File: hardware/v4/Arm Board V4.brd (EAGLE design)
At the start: 108 x 50.8 mm, 38 parts, among them IC3 L6206D, P1 STELLARIS-LAUNCHPADSTELLARIS-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, U1 SN74LS241DW, U2 XBEE-1B3

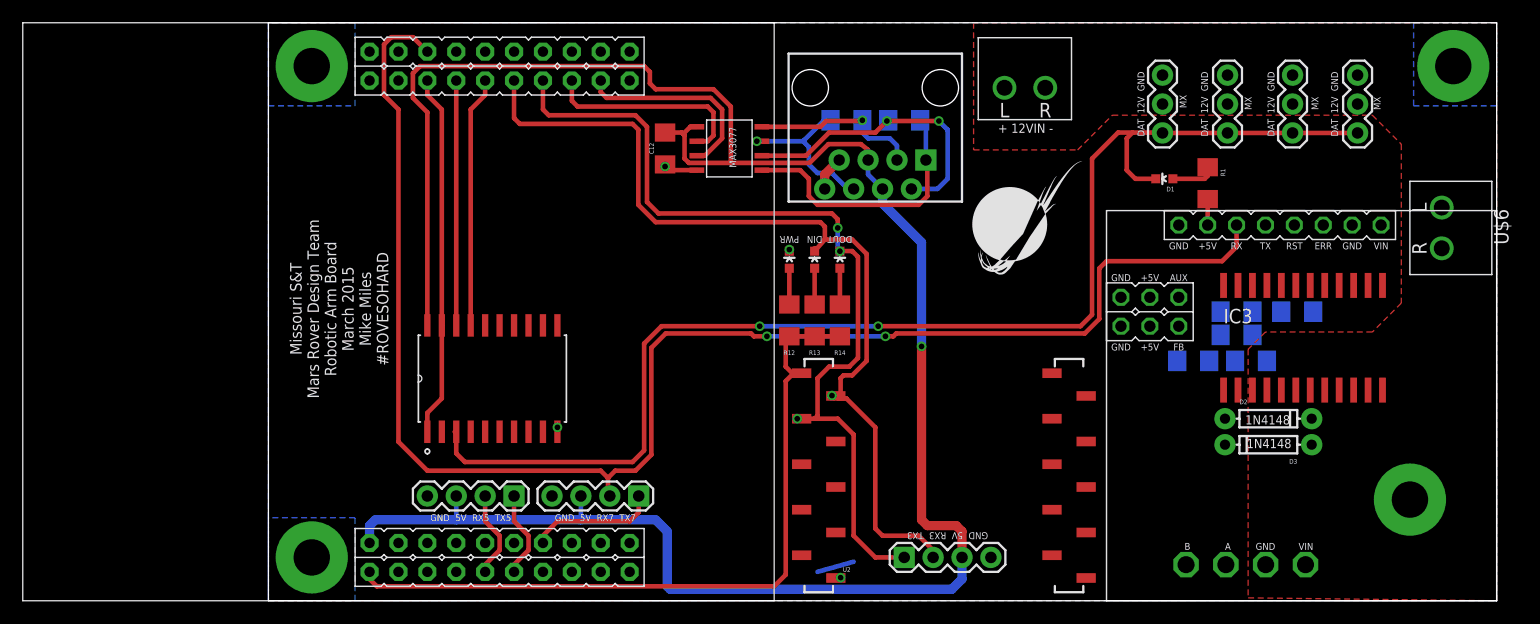
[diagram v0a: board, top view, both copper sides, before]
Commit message: arm board
added parts to allow linear actuator control with H-bridge in case servo
driver fails
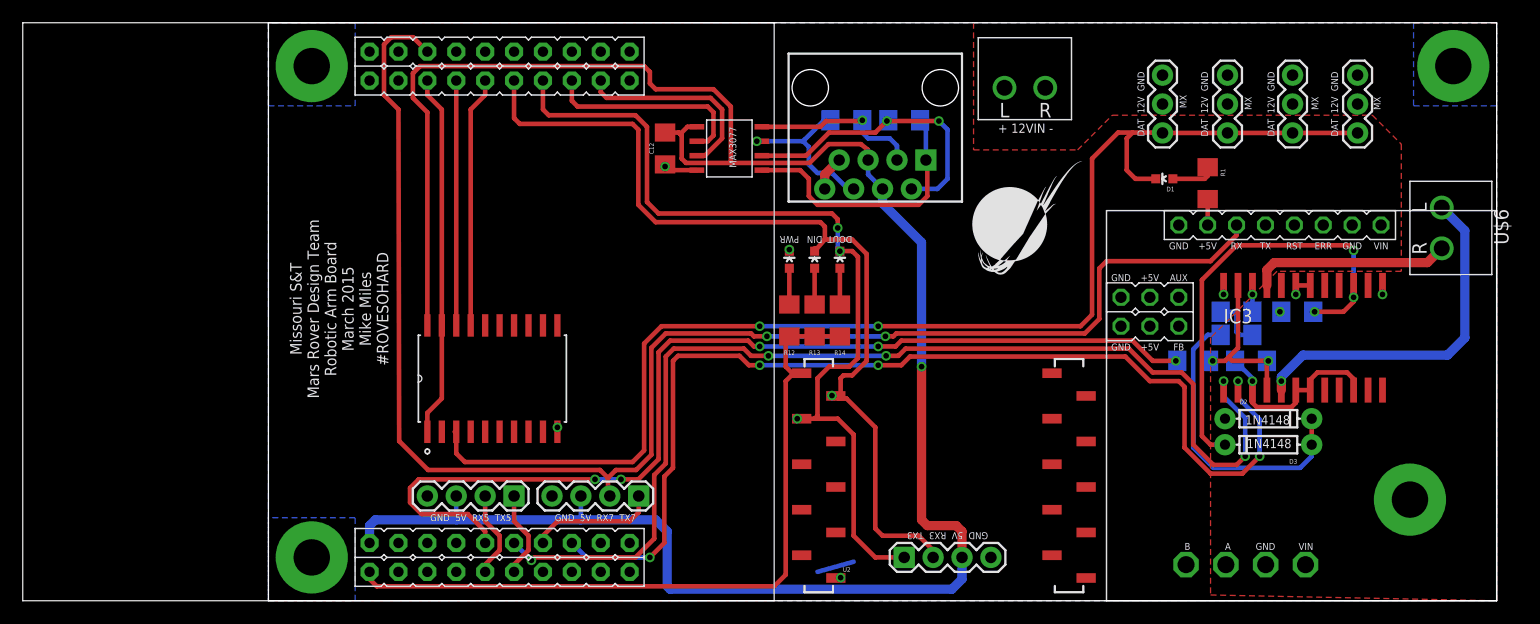
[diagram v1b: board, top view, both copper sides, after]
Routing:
- net IN1_A: track 0.00 -> 97.8 mm, vias 0 -> 5
- net IN2_A: track 0.00 -> 94.1 mm, vias 0 -> 5
- net EN_A: track 0.00 -> 89.7 mm, vias 0 -> 5
- net VBOOT: track 0.00 -> 40.3 mm, vias 0 -> 3
- net A1: track 0.00 -> 31.0 mm, vias 0 -> 1
- net N$17: track 0.00 -> 26.4 mm, vias 0 -> 1
- net GND: track 10.5 -> 31.2 mm, vias 4 -> 8
- net A2: track 0.00 -> 17.5 mm
- net OCD_A: track 0.00 -> 14.7 mm, vias 0 -> 2
- net N$18: track 0.00 -> 4.53 mm
- net N$19: track 0.00 -> 2.32 mm, vias 0 -> 1
- net RX_7: track 135.3 -> 134.6 mm
- net +12V: track 0.00 -> 0.12 mm, vias 0 -> 1

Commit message: about to reroute brd
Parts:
- moved R1 3.86 mm to (78.9, 35.6), turned to 0 degrees
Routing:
- net +5V: track 189.4 -> 191.2 mm
- net N$13: track 3.93 -> 2.65 mm
- net DDATA_1: track 113.5 -> 114.7 mm
- net TX_3: track 77.5 -> 78.5 mm
- net RX_3: track 80.9 -> 81.6 mm
- net GND: track 31.2 -> 31.7 mm
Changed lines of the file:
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@@
 <layer number="21" name="tPlace" color="7" fill="1" visible="yes" active="yes"/>
 <layer number="22" name="bPlace" color="7" fill="1" visible="yes" active="yes"/>
-<layer number="23" name="tOrigins" color="15" fill="1" visible="no" active="yes"/>
-<layer number="24" name="bOrigins" color="15" fill="1" visible="no" active="yes"/>
+<layer number="23" name="tOrigins" color="15" fill="1" visible="yes" active="yes"/>
+<layer number="24" name="bOrigins" color="15" fill="1" visible="yes" active="yes"/>
 <layer number="25" name="tNames" color="7" fill="1" visible="no" active="yes"/>
 <layer number="26" name="bNames" color="7" fill="1" visible="no" active="yes"/>
@@
 </element>
 <element name="U$1" library="MRDT-RoboticArm" package="TORXIS_BREAKOUT" value="TORXIS_BREAKOUT" x="107.95" y="0" rot="R90"/>
-<element name="R1" library="SparkFun-Resistors" package="1206" value="1k" x="82.55" y="36.703" rot="R270"/>
+<element name="R1" library="SparkFun-Resistors" package="1206" value="1k" x="78.867" y="35.56"/>
 <element name="D1" library="SparkFun-LED" package="LED-0603" value="RED" x="78.74" y="37.084" rot="R90">
 <attribute name="PROD_ID" value="DIO-00819" x="78.74" y="37.084" size="1.778" layer="27" rot="R90" display="off"/>
@@
 <via x="34.8615" y="38.1635" extent="1-16" drill="0.5"/>
 <wire x1="34.8615" y1="38.351" x2="34.8615" y2="38.1635" width="0.4064" layer="1"/>
-<via x="25.4" y="15.24" extent="1-16" drill="0.5"/>
-<wire x1="25.4" y1="15.24" x2="25.4" y2="14.85265" width="0.4064" layer="1"/>
-<via x="50.292" y="2.032" extent="1-16" drill="0.5"/>
-<wire x1="50.292" y1="2.032" x2="49.902" y2="2.032" width="0.4064" layer="1"/>
+<via x="25.4" y="15.5575" extent="1-16" drill="0.5"/>
+<wire x1="25.4" y1="15.5575" x2="25.4" y2="14.85265" width="0.4064" layer="1"/>
+<via x="49.276" y="2.032" extent="1-16" drill="0.5"/>
+<wire x1="49.276" y1="2.032" x2="49.902" y2="2.032" width="0.4064" layer="1"/>
 <wire x1="49.902" y1="2.032" x2="49.87" y2="2" width="0.4064" layer="1"/>
 <wire x1="48.895" y1="36.195" x2="48.895" y2="37.465" width="0.8128" layer="1"/>
@@
 <contactref element="R1" pad="2"/>
 <contactref element="U$1" pad="+5V_OUT"/>
-<wire x1="82.55" y1="33.02" x2="82.55" y2="35.303" width="0.4064" layer="1"/>
 <wire x1="37.6555" y1="41.656" x2="36.83" y2="41.656" width="0.4064" layer="1"/>
 <wire x1="27.432" y1="9.23925" x2="27.432" y2="9.17575" width="0.4064" layer="16"/>
@@
 <wire x1="34.8645" y1="41.148" x2="34.8615" y2="41.151" width="0.4064" layer="1"/>
 <wire x1="36.83" y1="41.656" x2="36.195" y2="41.021" width="0.4064" layer="1"/>
-<wire x1="57.404" y1="31.496" x2="82.55" y2="33.02" width="0" layer="19" extent="16-16"/>
+<wire x1="82.55" y1="33.02" x2="82.55" y2="34.29" width="0.4064" layer="1"/>
+<wire x1="82.55" y1="34.29" x2="81.28" y2="35.56" width="0.4064" layer="1"/>
+<wire x1="81.28" y1="35.56" x2="80.267" y2="35.56" width="0.4064" layer="1"/>
+<wire x1="57.404" y1="31.496" x2="80.267" y2="35.56" width="0" layer="19" extent="1-16"/>
 </signal>
 <signal name="+12V">
@@
 <wire x1="49.65" y1="17.78" x2="49.87" y2="18" width="0.4064" layer="1"/>
 <wire x1="21.59" y1="45.72" x2="21.59" y2="42.418" width="0.4064" layer="1"/>
-<wire x1="49.53" y1="17.78" x2="49.53" y2="18.034" width="0.4064" layer="1"/>
-<via x="49.53" y="18.034" extent="1-16" drill="0.5"/>
+<wire x1="49.53" y1="17.78" x2="49.276" y2="18.034" width="0.4064" layer="1"/>
+<via x="49.276" y="18.034" extent="1-16" drill="0.5"/>
 <wire x1="22.098" y1="41.91" x2="21.59" y2="42.418" width="0.4064" layer="1"/>
 <wire x1="32.004" y1="41.91" x2="22.098" y2="41.91" width="0.4064" layer="1"/>
-<wire x1="49.784" y1="18.034" x2="49.53" y2="18.034" width="0.4064" layer="1"/>
-<wire x1="49.53" y1="18.034" x2="50.292" y2="18.034" width="0.4064" layer="1"/>
+<wire x1="49.784" y1="18.034" x2="49.276" y2="18.034" width="0.4064" layer="1"/>
+<wire x1="49.276" y1="18.034" x2="50.292" y2="18.034" width="0.4064" layer="1"/>
 <wire x1="50.292" y1="18.034" x2="50.292" y2="19.558" width="0.4064" layer="1"/>
 <wire x1="50.292" y1="19.558" x2="50.546" y2="19.812" width="0.4064" layer="1"/>
@@
 <wire x1="46.87" y1="16" x2="47.5" y2="16" width="0.4064" layer="1"/>
 <wire x1="46.87" y1="16" x2="46.484" y2="16" width="0.4064" layer="1"/>
-<wire x1="46.484" y1="16" x2="46.482" y2="16.002" width="0.4064" layer="1"/>
-<via x="46.482" y="16.002" extent="1-16" drill="0.5"/>
+<wire x1="46.484" y1="16" x2="47.498" y2="16.002" width="0.4064" layer="1"/>
+<via x="47.498" y="16.002" extent="1-16" drill="0.5"/>
 <wire x1="50.04" y1="16" x2="48.006" y2="16" width="0.4064" layer="1"/>
 <wire x1="48.006" y1="16" x2="47.5" y2="16" width="0.4064" layer="1"/>
@@
 <wire x1="75.438" y1="37.846" x2="75.438" y2="40.64" width="0.4064" layer="1"/>
 <wire x1="75.438" y1="40.64" x2="75.946" y2="41.148" width="0.4064" layer="1"/>
-<wire x1="16.38935" y1="14.85265" x2="15.24" y2="14.85265" width="0" layer="19" extent="1-1"/>
+<wire x1="16.38935" y1="14.85265" x2="15.24" y2="14.85265" width="0.4064" layer="1"/>
 </signal>
 <signal name="N$7">
@@
 <contactref element="R1" pad="1"/>
 <contactref element="D1" pad="A"/>
-<wire x1="82.55" y1="38.103" x2="82.55" y2="37.338" width="0.4064" layer="1"/>
-<wire x1="82.55" y1="37.338" x2="82.296" y2="37.084" width="0.4064" layer="1"/>
-<wire x1="82.296" y1="37.084" x2="79.49" y2="37.084" width="0.4064" layer="1"/>
+<wire x1="77.467" y1="35.56" x2="77.966" y2="35.56" width="0.4064" layer="1"/>
+<wire x1="77.966" y1="35.56" x2="79.49" y2="37.084" width="0.4064" layer="1"/>
 </signal>
 <signal name="A1">
@@
 <contactref element="IC3" pad="15"/>
 <via x="91.948" y="25.4" extent="1-16" drill="0.5"/>
-<wire x1="95.377" y1="27.714" x2="95.377" y2="26.67" width="0.4064" layer="1"/>
-<wire x1="95.377" y1="26.67" x2="95.377" y2="26.289" width="0.4064" layer="1"/>
+<wire x1="95.377" y1="27.714" x2="95.377" y2="26.924" width="0.4064" layer="1"/>
+<wire x1="95.377" y1="26.924" x2="95.377" y2="26.289" width="0.4064" layer="1"/>
 <wire x1="95.377" y1="26.289" x2="94.488" y2="25.4" width="0.4064" layer="1"/>
 <wire x1="94.488" y1="25.4" x2="91.948" y2="25.4" width="0.4064" layer="1"/>
@@
 <wire x1="94.9325" y1="31.242" x2="95.377" y2="30.7975" width="0.4064" layer="1"/>
 <via x="95.377" y="30.7975" extent="1-16" drill="0.5"/>
-<wire x1="95.377" y1="30.7975" x2="95.377" y2="26.67" width="0.4064" layer="16"/>
-<via x="95.377" y="26.67" extent="1-16" drill="0.5"/>
+<wire x1="95.377" y1="30.7975" x2="95.377" y2="26.924" width="0.4064" layer="16"/>
+<via x="95.377" y="26.924" extent="1-16" drill="0.5"/>
 </signal>
 </signals>

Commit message: didnt do much
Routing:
- net GND: track 31.7 -> 28.4 mm
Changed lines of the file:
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@@
 </polygon>
 <wire x1="49.87" y1="2" x2="50.006" y2="2" width="0.4064" layer="1"/>
-<wire x1="51.435" y1="3.429" x2="48.26" y2="2.54" width="0.4064" layer="16"/>
 <via x="45.7835" y="30.861" extent="1-16" drill="0.5"/>
 <wire x1="37.6555" y1="37.846" x2="35.3665" y2="37.846" width="0.4064" layer="1"/>

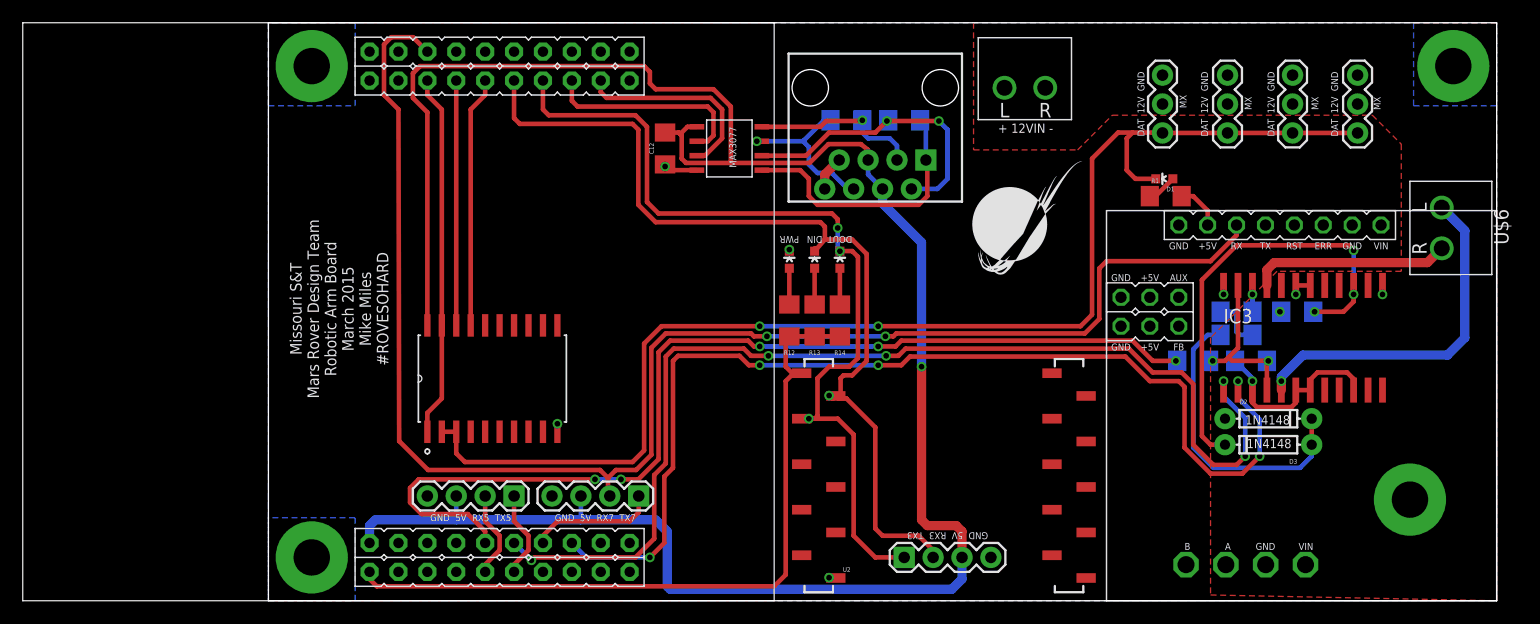
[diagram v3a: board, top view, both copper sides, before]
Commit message: cleaned up routes, swapped 603 LEDs for 1206
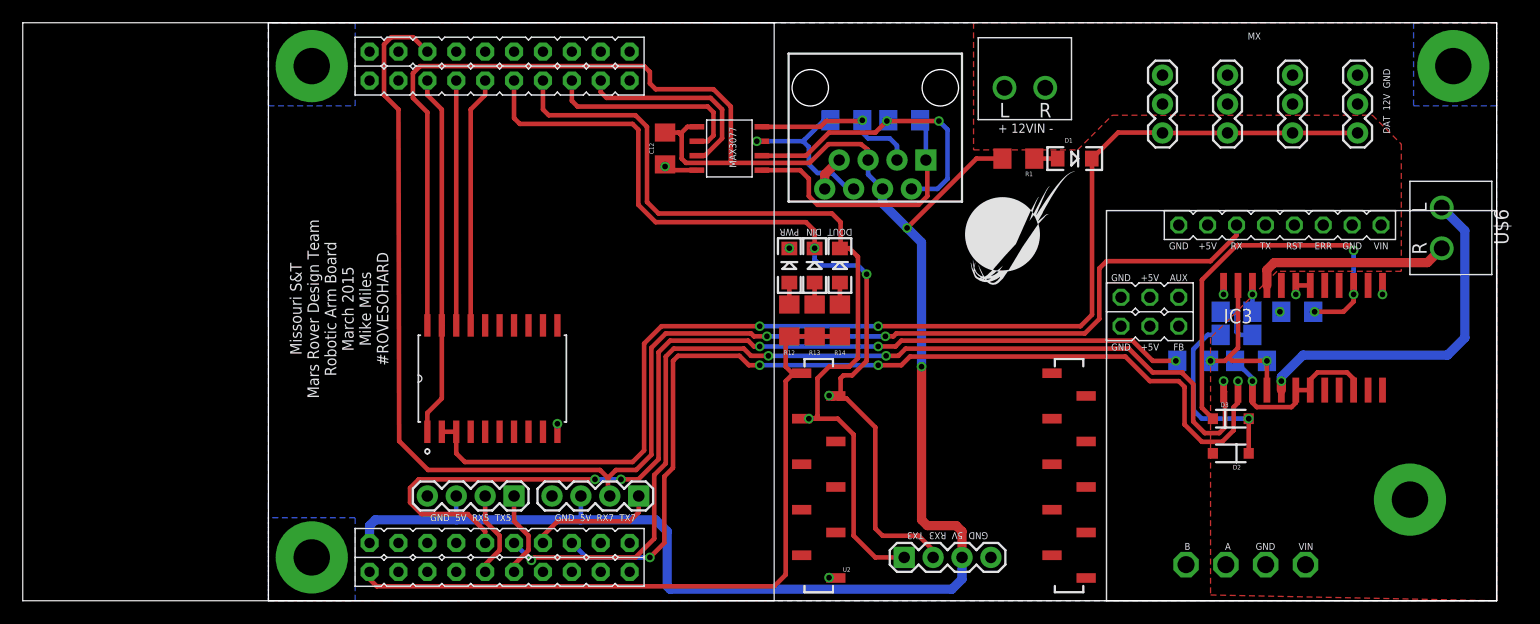
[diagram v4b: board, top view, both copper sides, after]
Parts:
- D1, LED1, LED2, LED3: device SparkFun-LED:LED-0603 -> SparkFun-LED:LED-1206
- D2, D3: device SparkFun-DiscreteSemi:DIODE-1N4148 -> SparkFun-DiscreteSemi:SOD-123
- JP10, JP11, JP12, JP9: value (none) -> DYNAMIXEL-1X03; device SparkFun-Connectors:1X03 -> MRDT-2015-Arm:DYNAMIXEL-1X03
- U$1: device MRDT-RoboticArm:TORXIS_BREAKOUT -> MRDT-2015-Arm:TORXIS_BREAKOUT
- moved R1 13.4 mm to (65.9, 38.9), turned to 180 degrees
- moved D1 8.07 mm to (70.9, 38.9), turned to 0 degrees
- moved D2 4.49 mm to (84.6, 13.0), turned to 180 degrees
- moved D3 4.02 mm to (84.6, 16.0), turned to 0 degrees
- moved LED1 0.51 mm to (45.8, 29.5), turned to 90 degrees
- moved LED2 0.51 mm to (48.0, 29.5), turned to 90 degrees
- moved LED3 0.51 mm to (50.2, 29.5), turned to 90 degrees
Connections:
- removed net N$11: U$1.GND@2
- removed net N$12: U$1.FB
- removed net N$21: U$1.A
- removed net N$22: U$1.B
- removed net N$9: U$1.+5V@1
- net +12V: now also JP10.VIN, JP11.VIN, JP12.VIN, JP9.VIN, U$1.VIN; no longer JP10.2, JP11.2, JP12.2, JP9.2
- net +5V: no longer U$1.+5V_OUT
- net DDATA_1: now also JP10.DDATA, JP11.DDATA, JP12.DDATA, JP9.DDATA; no longer JP10.3, JP11.3, JP12.3, JP9.3
- net GND: now also JP10.GND, JP11.GND, JP12.GND, JP9.GND, U$1.GND@1; no longer JP10.1, JP11.1, JP12.1, JP9.1, U$1.GND@4
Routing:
- net N$17: track 26.4 -> 16.5 mm
- net IN2_A: track 94.1 -> 85.6 mm, vias 5 -> 4
- net IN1_A: track 97.8 -> 89.5 mm, vias 5 -> 4
- net +5V: track 191.2 -> 198.0 mm, vias 1 -> 2
- net DDATA_1: track 114.7 -> 108.3 mm
- net VBOOT: track 40.1 -> 36.6 mm
- net RX_3: track 81.6 -> 79.7 mm, vias 1 -> 3
- net N$6: track 3.18 -> 1.93 mm
- net N$4: track 3.18 -> 1.93 mm
- net N$38: track 3.18 -> 1.93 mm
- net N$13: track 2.65 -> 2.05 mm
- net TX_3: track 78.5 -> 78.4 mm, vias 3 -> 1
